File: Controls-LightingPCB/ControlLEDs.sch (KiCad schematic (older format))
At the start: 18 parts

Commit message: Added HX1188FNL
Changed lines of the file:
@@
 $Descr A4 11693 8268
 encoding utf-8
-Sheet 4 4
+Sheet 3 4
 Title ""
 Date ""
@@
 U 1 1 5F7BCB61
 P 7900 4500
+AR Path="/5F7BCB61" Ref="D?"  Part="1"
+AR Path="/5F7A71E1/5F7BCB61" Ref="D?"  Part="1"
 F 0 "D?" V 7939 4383 50  0000 R CNN
 F 1 "RSVD_LED" V 7848 4383 50  0000 R CNN
@@
 U 1 1 5F7BCB67
 P 6900 2800
+AR Path="/5F7BCB67" Ref="D?"  Part="1"
+AR Path="/5F7A71E1/5F7BCB67" Ref="D?"  Part="1"
 F 0 "D?" V 6939 2683 50  0000 R CNN
 F 1 "CTRL_FAULT" V 6848 2683 50  0000 R CNN
@@
 U 1 1 5F7BCB6D
 P 5900 4500
+AR Path="/5F7BCB6D" Ref="D?"  Part="1"
+AR Path="/5F7A71E1/5F7BCB6D" Ref="D?"  Part="1"
 F 0 "D?" V 5939 4382 50  0000 R CNN
 F 1 "Headlight_ON" V 5848 4382 50  0000 R CNN
@@
 U 1 1 5F7BCB73
 P 7400 4500
+AR Path="/5F7BCB73" Ref="D?"  Part="1"
+AR Path="/5F7A71E1/5F7BCB73" Ref="D?"  Part="1"
 F 0 "D?" V 7439 4382 50  0000 R CNN
 F 1 "A_CNCTR" V 7348 4382 50  0000 R CNN
@@
 U 1 1 5F7BCB79
 P 5400 4500
+AR Path="/5F7BCB79" Ref="D?"  Part="1"
+AR Path="/5F7A71E1/5F7BCB79" Ref="D?"  Part="1"
 F 0 "D?" V 5439 4382 50  0000 R CNN
 F 1 "BPS_FAULT" V 5348 4382 50  0000 R CNN
@@
 U 1 1 5F7BCB7F
 P 4900 2800
+AR Path="/5F7BCB7F" Ref="D?"  Part="1"
+AR Path="/5F7A71E1/5F7BCB7F" Ref="D?"  Part="1"
 F 0 "D?" V 4939 2682 50  0000 R CNN
 F 1 "LEFT_BLINK" V 4848 2682 50  0000 R CNN
@@
 U 1 1 5F7BCB85
 P 7400 4100
+AR Path="/5F7BCB85" Ref="R?"  Part="1"
+AR Path="/5F7A71E1/5F7BCB85" Ref="R?"  Part="1"
 F 0 "R?" H 7470 4146 50  0000 L CNN
 F 1 "330R" H 7470 4055 50  0000 L CNN
@@
 U 1 1 5F7BCB8B
 P 7900 4100
+AR Path="/5F7BCB8B" Ref="R?"  Part="1"
+AR Path="/5F7A71E1/5F7BCB8B" Ref="R?"  Part="1"
 F 0 "R?" H 7970 4146 50  0000 L CNN
 F 1 "330R" H 7970 4055 50  0000 L CNN
@@
 U 1 1 5F7BCB91
 P 5900 4100
+AR Path="/5F7BCB91" Ref="R?"  Part="1"
+AR Path="/5F7A71E1/5F7BCB91" Ref="R?"  Part="1"
 F 0 "R?" H 5970 4146 50  0000 L CNN
 F 1 "330R" H 5970 4055 50  0000 L CNN
@@
 U 1 1 5F7BCB97
 P 6400 4100
+AR Path="/5F7BCB97" Ref="R?"  Part="1"
+AR Path="/5F7A71E1/5F7BCB97" Ref="R?"  Part="1"
 F 0 "R?" H 6470 4146 50  0000 L CNN
 F 1 "330R" H 6470 4055 50  0000 L CNN
@@
 U 1 1 5F7BCB9D
 P 6900 2400
+AR Path="/5F7BCB9D" Ref="R?"  Part="1"
+AR Path="/5F7A71E1/5F7BCB9D" Ref="R?"  Part="1"
 F 0 "R?" H 6970 2446 50  0000 L CNN
 F 1 "330R" H 6970 2355 50  0000 L CNN
@@
 U 1 1 5F7BCBA3
 P 4400 4100
+AR Path="/5F7BCBA3" Ref="R?"  Part="1"
+AR Path="/5F7A71E1/5F7BCBA3" Ref="R?"  Part="1"
 F 0 "R?" H 4470 4146 50  0000 L CNN
 F 1 "1.2k" H 4470 4055 50  0000 L CNN
@@
 U 1 1 5F7BCBA9
 P 4900 2400
+AR Path="/5F7BCBA9" Ref="R?"  Part="1"
+AR Path="/5F7A71E1/5F7BCBA9" Ref="R?"  Part="1"
 F 0 "R?" H 4970 2446 50  0000 L CNN
 F 1 "330R" H 4970 2355 50  0000 L CNN
@@
 U 1 1 5F7BCBAF
 P 5400 4100
+AR Path="/5F7BCBAF" Ref="R?"  Part="1"
+AR Path="/5F7A71E1/5F7BCBAF" Ref="R?"  Part="1"
 F 0 "R?" H 5470 4146 50  0000 L CNN
 F 1 "330R" H 5470 4055 50  0000 L CNN
@@
 U 1 1 5F7BCBB5
 P 4400 4500
+AR Path="/5F7BCBB5" Ref="D?"  Part="1"
+AR Path="/5F7A71E1/5F7BCBB5" Ref="D?"  Part="1"
 F 0 "D?" V 4439 4383 50  0000 R CNN
 F 1 "BPS_PWR" V 4348 4383 50  0000 R CNN
@@
 U 1 1 5F7BCBBB
 P 3900 2050
+AR Path="/5F7BCBBB" Ref="#PWR?"  Part="1"
+AR Path="/5F7A71E1/5F7BCBBB" Ref="#PWR?"  Part="1"
 F 0 "#PWR?" H 3900 1900 50  0001 C CNN
 F 1 "+3.3V" H 3915 2223 50  0000 C CNN
@@
 U 1 1 5F7BCBC1
 P 3900 4900
+AR Path="/5F7BCBC1" Ref="#PWR?"  Part="1"
+AR Path="/5F7A71E1/5F7BCBC1" Ref="#PWR?"  Part="1"
 F 0 "#PWR?" H 3900 4700 50  0001 C CNN
 F 1 "GNDPWR" H 3904 4746 50  0000 C CNN
@@
 $EndComp
 Wire Wire Line
-	3900 2950 3600 2950
-Wire Wire Line
 	7900 4250 7900 4350
 Wire Wire Line
@@
 Wire Wire Line
 	4400 4250 4400 4350
-Wire Wire Line
-	3600 3950 3900 3950
-Wire Wire Line
-	3900 2150 3900 2950
 $Comp
 L Device:LED D?
 U 1 1 5F7BCBD1
 P 8400 4500
+AR Path="/5F7BCBD1" Ref="D?"  Part="1"
+AR Path="/5F7A71E1/5F7BCBD1" Ref="D?"  Part="1"
 F 0 "D?" V 8439 4383 50  0000 R CNN
 F 1 "M_CNCTR" V 8348 4383 50  0000 R CNN
@@
 U 1 1 5F7BCBD8
 P 8400 4100
+AR Path="/5F7BCBD8" Ref="R?"  Part="1"
+AR Path="/5F7A71E1/5F7BCBD8" Ref="R?"  Part="1"
 F 0 "R?" H 8470 4146 50  0000 L CNN
 F 1 "330R" H 8470 4055 50  0000 L CNN
@@
 	8400 3050 8400 3950
 Wire Wire Line
-	3900 3950 3900 4800
-Wire Wire Line
 	4400 4650 4400 4800
 Wire Wire Line
 	4400 4800 3900 4800
-Connection ~ 3900 4800
 Wire Wire Line
 	3900 4800 3900 4900
@@
 Wire Wire Line
 	6900 2150 4900 2150
-Connection ~ 3900 2150
 Wire Wire Line
 	3900 2150 3900 2050
@@
 U 1 1 5F7BCC0D
 P 6400 4500
+AR Path="/5F7BCC0D" Ref="D?"  Part="1"
+AR Path="/5F7A71E1/5F7BCC0D" Ref="D?"  Part="1"
 F 0 "D?" V 6439 4383 50  0000 R CNN
 F 1 "RIGHT_BLINK" V 6348 4383 50  0000 R CNN
@@
 Wire Wire Line
 	6400 4250 6400 4350
-Text HLabel 3600 2950 0    50   UnSpc ~ 0
-+3.3V
 Text HLabel 3600 3050 0    50   Output ~ 0
 M_CNCTR
@@
 Text HLabel 3600 3850 0    50   Output ~ 0
 BPS_PWR
-Text HLabel 3600 3950 0    50   UnSpc ~ 0
-GND
 $EndSCHEMATC

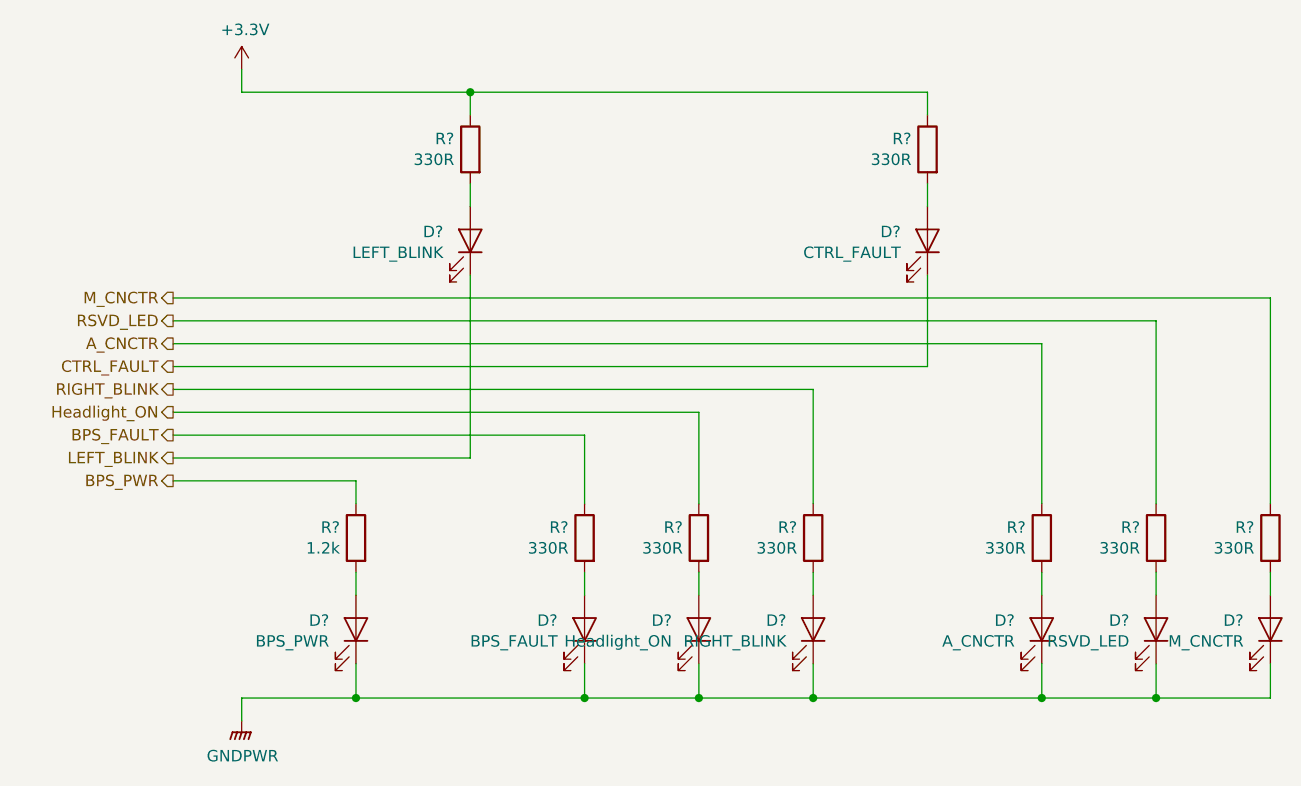
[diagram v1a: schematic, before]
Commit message: Started working on PCD design, preliminary layout of components
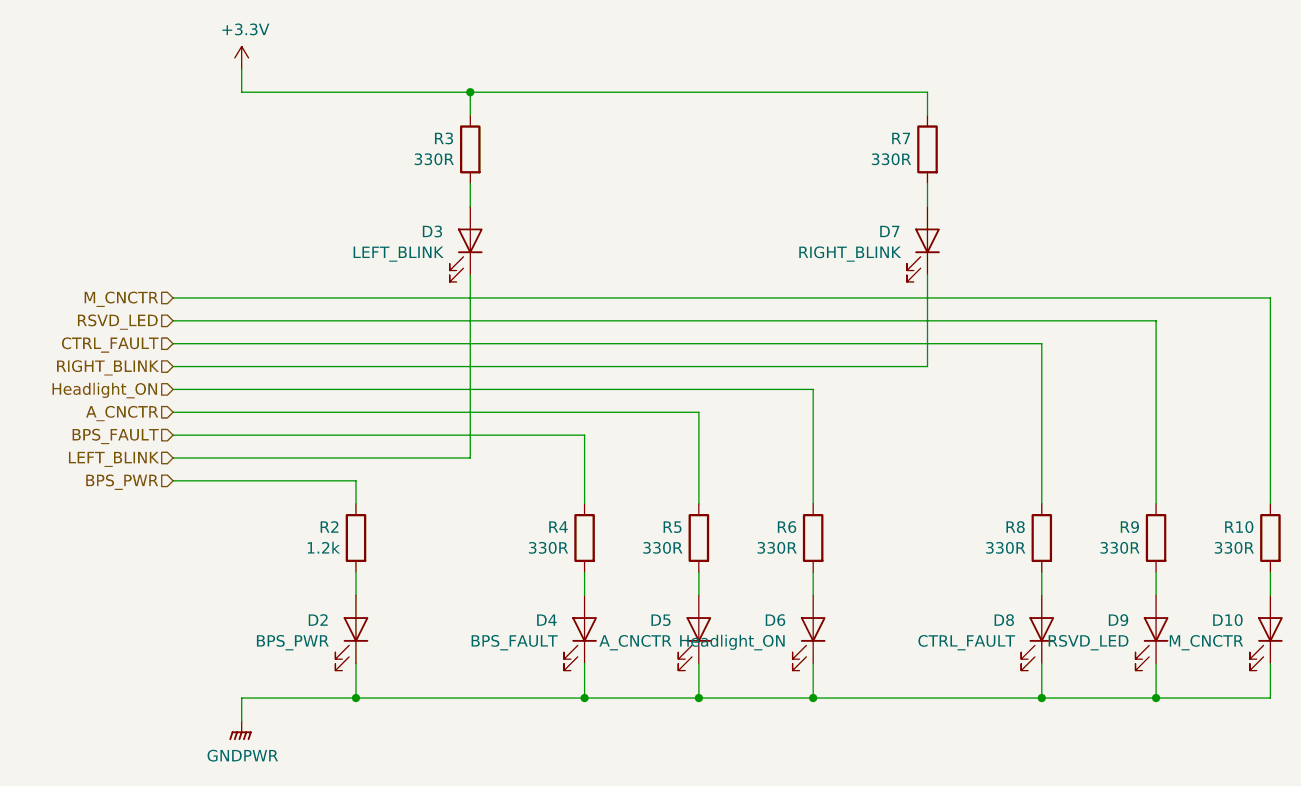
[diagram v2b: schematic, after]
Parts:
- gave numbers to parts that had none: 18
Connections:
- net +3V3: now also R7.1; no longer R5.1
- net A_CNCTR: now also R5.1; no longer R8.1
- net CTRL_FAULT: now also R8.1; no longer D8.1 (K)
- net GNDPWR: now also D8.1 (K); no longer D7.1 (K)
- net RIGHT_BLINK: now also D7.1 (K); no longer R7.1
- net at D8.2 (A): now also R8.2; no longer R5.2
- net at D5.2 (A): now also R5.2; no longer R8.2
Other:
- moved on the sheet: D5, D6, D7, D8, R5, R6, R7
